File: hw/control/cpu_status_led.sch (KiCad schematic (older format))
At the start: 4 parts, among them Q401 BC817

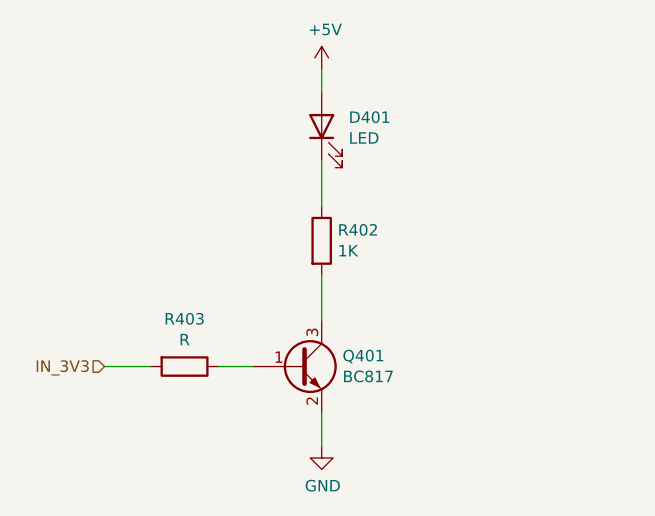
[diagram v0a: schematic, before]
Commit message: i[hw] Add IIS audio module connector
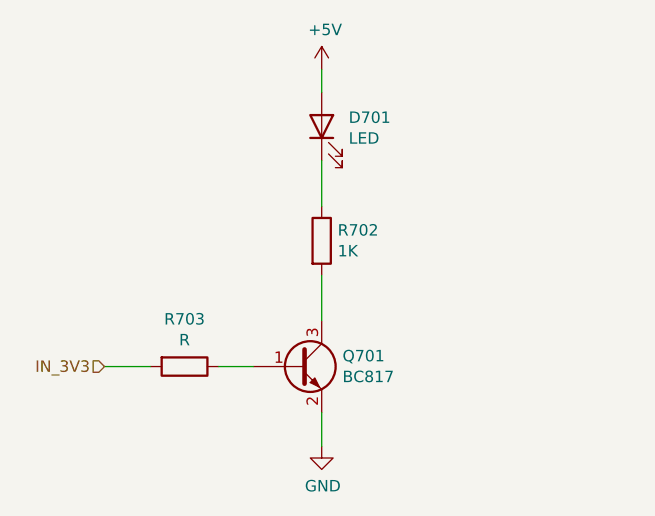
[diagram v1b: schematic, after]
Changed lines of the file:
@@
 AR Path="/6148E1AC/61836CD9/6182751A" Ref="#PWR0601"  Part="1"
 AR Path="/6148E1AC/61844B10/6182751A" Ref="#PWR0701"  Part="1"
-F 0 "#PWR0401" H 5500 2550 50  0001 C CNN
+F 0 "#PWR0701" H 5500 2550 50  0001 C CNN
 F 1 "+5V" H 5515 2873 50  0000 C CNN
 F 2 "" H 5500 2700 50  0001 C CNN
@@
 AR Path="/6148E1AC/61836CD9/6182D735" Ref="R603"  Part="1"
 AR Path="/6148E1AC/61844B10/6182D735" Ref="R703"  Part="1"
-F 0 "R403" V 4693 4000 50  0000 C CNN
+F 0 "R703" V 4693 4000 50  0000 C CNN
 F 1 "R" V 4784 4000 50  0000 C CNN
 F 2 "Resistor_SMD:R_0805_2012Metric_Pad1.20x1.40mm_HandSolder" V 4830 4000 50  0001 C CNN
@@
 AR Path="/6148E1AC/61836CD9/6182D73B" Ref="Q601"  Part="1"
 AR Path="/6148E1AC/61844B10/6182D73B" Ref="Q701"  Part="1"
-F 0 "Q401" H 5591 4046 50  0000 L CNN
+F 0 "Q701" H 5591 4046 50  0000 L CNN
 F 1 "BC817" H 5591 3955 50  0000 L CNN
 F 2 "Package_TO_SOT_SMD:SOT-23_Handsoldering" H 5600 4100 50  0001 C CNN
@@
 AR Path="/6148E1AC/61836CD9/6182D99B" Ref="D601"  Part="1"
 AR Path="/6148E1AC/61844B10/6182D99B" Ref="D701"  Part="1"
-F 0 "D401" V 5539 2832 50  0000 R CNN
+F 0 "D701" V 5539 2832 50  0000 R CNN
 F 1 "LED" V 5448 2832 50  0000 R CNN
 F 2 "LED_SMD:LED_0805_2012Metric_Pad1.15x1.40mm_HandSolder" H 5500 2950 50  0001 C CNN
@@
 AR Path="/6148E1AC/61836CD9/6182E435" Ref="R602"  Part="1"
 AR Path="/6148E1AC/61844B10/6182E435" Ref="R702"  Part="1"
-F 0 "R402" H 5570 3496 50  0000 L CNN
+F 0 "R702" H 5570 3496 50  0000 L CNN
 F 1 "1K" H 5570 3405 50  0000 L CNN
 F 2 "Resistor_SMD:R_0805_2012Metric_Pad1.20x1.40mm_HandSolder" V 5430 3450 50  0001 C CNN
@@
 AR Path="/6148E1AC/61836CD9/6182FC68" Ref="#PWR0602"  Part="1"
 AR Path="/6148E1AC/61844B10/6182FC68" Ref="#PWR0702"  Part="1"
-F 0 "#PWR0402" H 5500 4100 50  0001 C CNN
+F 0 "#PWR0702" H 5500 4100 50  0001 C CNN
 F 1 "GND" H 5505 4177 50  0000 C CNN
 F 2 "" H 5500 4350 50  0001 C CNN

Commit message: [hw] Add button, move sd card
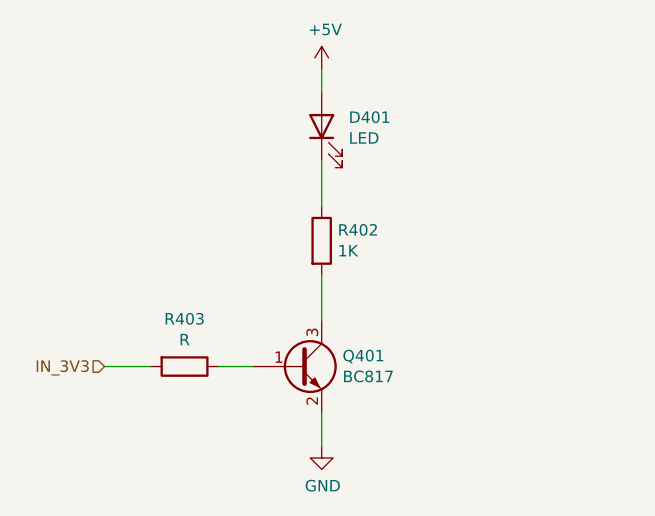
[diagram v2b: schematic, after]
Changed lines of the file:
@@
 AR Path="/6148E1AC/61836CD9/6182D735" Ref="R603"  Part="1"
 AR Path="/6148E1AC/61844B10/6182D735" Ref="R703"  Part="1"
-F 0 "R703" V 4693 4000 50  0000 C CNN
+F 0 "R403" V 4693 4000 50  0000 C CNN
 F 1 "R" V 4784 4000 50  0000 C CNN
 F 2 "Resistor_SMD:R_0805_2012Metric_Pad1.20x1.40mm_HandSolder" V 4830 4000 50  0001 C CNN
@@
 AR Path="/6148E1AC/61836CD9/6182D73B" Ref="Q601"  Part="1"
 AR Path="/6148E1AC/61844B10/6182D73B" Ref="Q701"  Part="1"
-F 0 "Q701" H 5591 4046 50  0000 L CNN
+F 0 "Q401" H 5591 4046 50  0000 L CNN
 F 1 "BC817" H 5591 3955 50  0000 L CNN
 F 2 "Package_TO_SOT_SMD:SOT-23_Handsoldering" H 5600 4100 50  0001 C CNN
@@
 AR Path="/6148E1AC/61836CD9/6182D99B" Ref="D601"  Part="1"
 AR Path="/6148E1AC/61844B10/6182D99B" Ref="D701"  Part="1"
-F 0 "D701" V 5539 2832 50  0000 R CNN
+F 0 "D401" V 5539 2832 50  0000 R CNN
 F 1 "LED" V 5448 2832 50  0000 R CNN
 F 2 "LED_SMD:LED_0805_2012Metric_Pad1.15x1.40mm_HandSolder" H 5500 2950 50  0001 C CNN
@@
 AR Path="/6148E1AC/61836CD9/6182E435" Ref="R602"  Part="1"
 AR Path="/6148E1AC/61844B10/6182E435" Ref="R702"  Part="1"
-F 0 "R702" H 5570 3496 50  0000 L CNN
+F 0 "R402" H 5570 3496 50  0000 L CNN
 F 1 "1K" H 5570 3405 50  0000 L CNN
 F 2 "Resistor_SMD:R_0805_2012Metric_Pad1.20x1.40mm_HandSolder" V 5430 3450 50  0001 C CNN

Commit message: [hw] Isolate SD card holder shield from ground
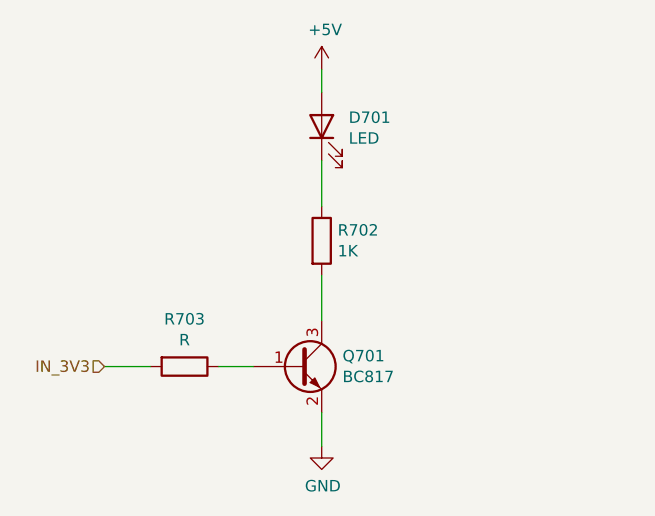
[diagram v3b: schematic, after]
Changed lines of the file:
@@
 AR Path="/6148E1AC/61836CD9/6182D735" Ref="R603"  Part="1"
 AR Path="/6148E1AC/61844B10/6182D735" Ref="R703"  Part="1"
-F 0 "R403" V 4693 4000 50  0000 C CNN
+F 0 "R703" V 4693 4000 50  0000 C CNN
 F 1 "R" V 4784 4000 50  0000 C CNN
 F 2 "Resistor_SMD:R_0805_2012Metric_Pad1.20x1.40mm_HandSolder" V 4830 4000 50  0001 C CNN
@@
 AR Path="/6148E1AC/61836CD9/6182D73B" Ref="Q601"  Part="1"
 AR Path="/6148E1AC/61844B10/6182D73B" Ref="Q701"  Part="1"
-F 0 "Q401" H 5591 4046 50  0000 L CNN
+F 0 "Q701" H 5591 4046 50  0000 L CNN
 F 1 "BC817" H 5591 3955 50  0000 L CNN
 F 2 "Package_TO_SOT_SMD:SOT-23_Handsoldering" H 5600 4100 50  0001 C CNN
@@
 AR Path="/6148E1AC/61836CD9/6182D99B" Ref="D601"  Part="1"
 AR Path="/6148E1AC/61844B10/6182D99B" Ref="D701"  Part="1"
-F 0 "D401" V 5539 2832 50  0000 R CNN
+F 0 "D701" V 5539 2832 50  0000 R CNN
 F 1 "LED" V 5448 2832 50  0000 R CNN
 F 2 "LED_SMD:LED_0805_2012Metric_Pad1.15x1.40mm_HandSolder" H 5500 2950 50  0001 C CNN
@@
 AR Path="/6148E1AC/61836CD9/6182E435" Ref="R602"  Part="1"
 AR Path="/6148E1AC/61844B10/6182E435" Ref="R702"  Part="1"
-F 0 "R402" H 5570 3496 50  0000 L CNN
+F 0 "R702" H 5570 3496 50  0000 L CNN
 F 1 "1K" H 5570 3405 50  0000 L CNN
 F 2 "Resistor_SMD:R_0805_2012Metric_Pad1.20x1.40mm_HandSolder" V 5430 3450 50  0001 C CNN

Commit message: [hw] Re-annotate all components
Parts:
- renumbered R402 to R401, R403 to R402
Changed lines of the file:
@@
 AR Path="/614AE8DA/6182D735" Ref="R?"  Part="1"
 AR Path="/614AB031/6182D735" Ref="R?"  Part="1"
-AR Path="/6148E1AC/6182662F/6182D735" Ref="R403"  Part="1"
-AR Path="/6148E1AC/61831583/6182D735" Ref="R503"  Part="1"
-AR Path="/6148E1AC/61836CD9/6182D735" Ref="R603"  Part="1"
-AR Path="/6148E1AC/61844B10/6182D735" Ref="R703"  Part="1"
-F 0 "R703" V 4693 4000 50  0000 C CNN
+AR Path="/6148E1AC/6182662F/6182D735" Ref="R402"  Part="1"
+AR Path="/6148E1AC/61831583/6182D735" Ref="R502"  Part="1"
+AR Path="/6148E1AC/61836CD9/6182D735" Ref="R602"  Part="1"
+AR Path="/6148E1AC/61844B10/6182D735" Ref="R702"  Part="1"
+F 0 "R702" V 4693 4000 50  0000 C CNN
 F 1 "R" V 4784 4000 50  0000 C CNN
 F 2 "Resistor_SMD:R_0805_2012Metric_Pad1.20x1.40mm_HandSolder" V 4830 4000 50  0001 C CNN
@@
 $EndComp
 $Comp
-L Device:R R402
+L Device:R R401
 U 1 1 6182E435
 P 5500 3450
-AR Path="/6148E1AC/6182662F/6182E435" Ref="R402"  Part="1"
-AR Path="/6148E1AC/61831583/6182E435" Ref="R502"  Part="1"
-AR Path="/6148E1AC/61836CD9/6182E435" Ref="R602"  Part="1"
-AR Path="/6148E1AC/61844B10/6182E435" Ref="R702"  Part="1"
-F 0 "R702" H 5570 3496 50  0000 L CNN
+AR Path="/6148E1AC/6182662F/6182E435" Ref="R401"  Part="1"
+AR Path="/6148E1AC/61831583/6182E435" Ref="R501"  Part="1"
+AR Path="/6148E1AC/61836CD9/6182E435" Ref="R601"  Part="1"
+AR Path="/6148E1AC/61844B10/6182E435" Ref="R701"  Part="1"
+F 0 "R701" H 5570 3496 50  0000 L CNN
 F 1 "1K" H 5570 3405 50  0000 L CNN
 F 2 "Resistor_SMD:R_0805_2012Metric_Pad1.20x1.40mm_HandSolder" V 5430 3450 50  0001 C CNN

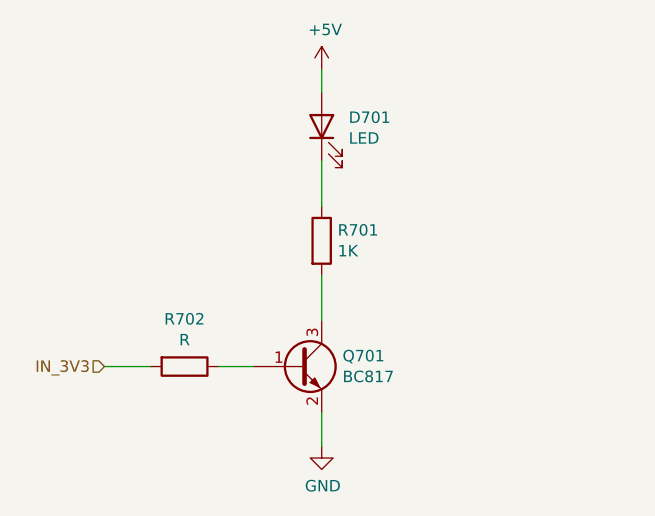
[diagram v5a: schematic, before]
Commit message: [hw] Add missing resistor values
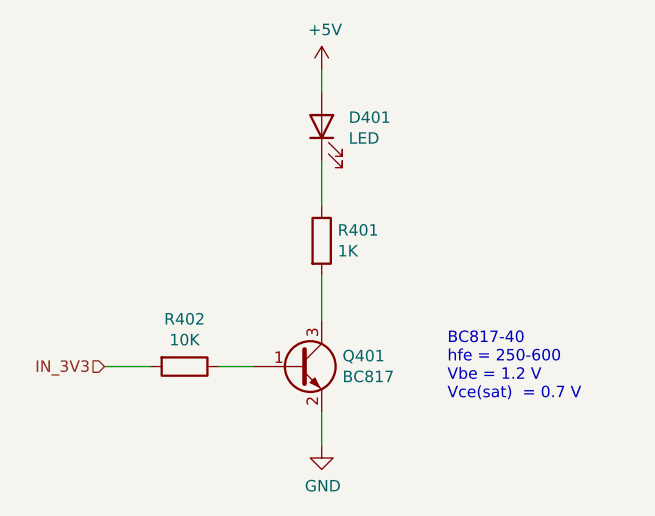
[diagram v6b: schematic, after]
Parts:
- R402: value R -> 10K
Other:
- note added: "BC817-40\nhfe = 250-600\nVbe = 1.2 V\nVce(sat) = 0.7 V"
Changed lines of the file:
@@
 AR Path="/6148E1AC/61836CD9/6182751A" Ref="#PWR0601"  Part="1"
 AR Path="/6148E1AC/61844B10/6182751A" Ref="#PWR0701"  Part="1"
-F 0 "#PWR0701" H 5500 2550 50  0001 C CNN
+F 0 "#PWR0401" H 5500 2550 50  0001 C CNN
 F 1 "+5V" H 5515 2873 50  0000 C CNN
 F 2 "" H 5500 2700 50  0001 C CNN
@@
 AR Path="/6148E1AC/61836CD9/6182D735" Ref="R602"  Part="1"
 AR Path="/6148E1AC/61844B10/6182D735" Ref="R702"  Part="1"
-F 0 "R702" V 4693 4000 50  0000 C CNN
-F 1 "R" V 4784 4000 50  0000 C CNN
+F 0 "R402" V 4693 4000 50  0000 C CNN
+F 1 "10K" V 4784 4000 50  0000 C CNN
 F 2 "Resistor_SMD:R_0805_2012Metric_Pad1.20x1.40mm_HandSolder" V 4830 4000 50  0001 C CNN
 F 3 "~" H 4900 4000 50  0001 C CNN
@@
 AR Path="/6148E1AC/61836CD9/6182D73B" Ref="Q601"  Part="1"
 AR Path="/6148E1AC/61844B10/6182D73B" Ref="Q701"  Part="1"
-F 0 "Q701" H 5591 4046 50  0000 L CNN
+F 0 "Q401" H 5591 4046 50  0000 L CNN
 F 1 "BC817" H 5591 3955 50  0000 L CNN
 F 2 "Package_TO_SOT_SMD:SOT-23_Handsoldering" H 5600 4100 50  0001 C CNN
@@
 AR Path="/6148E1AC/61836CD9/6182D99B" Ref="D601"  Part="1"
 AR Path="/6148E1AC/61844B10/6182D99B" Ref="D701"  Part="1"
-F 0 "D701" V 5539 2832 50  0000 R CNN
+F 0 "D401" V 5539 2832 50  0000 R CNN
 F 1 "LED" V 5448 2832 50  0000 R CNN
 F 2 "LED_SMD:LED_0805_2012Metric_Pad1.15x1.40mm_HandSolder" H 5500 2950 50  0001 C CNN
@@
 AR Path="/6148E1AC/61836CD9/6182E435" Ref="R601"  Part="1"
 AR Path="/6148E1AC/61844B10/6182E435" Ref="R701"  Part="1"
-F 0 "R701" H 5570 3496 50  0000 L CNN
+F 0 "R401" H 5570 3496 50  0000 L CNN
 F 1 "1K" H 5570 3405 50  0000 L CNN
 F 2 "Resistor_SMD:R_0805_2012Metric_Pad1.20x1.40mm_HandSolder" V 5430 3450 50  0001 C CNN
@@
 AR Path="/6148E1AC/61836CD9/6182FC68" Ref="#PWR0602"  Part="1"
 AR Path="/6148E1AC/61844B10/6182FC68" Ref="#PWR0702"  Part="1"
-F 0 "#PWR0702" H 5500 4100 50  0001 C CNN
+F 0 "#PWR0402" H 5500 4100 50  0001 C CNN
 F 1 "GND" H 5505 4177 50  0000 C CNN
 F 2 "" H 5500 4350 50  0001 C CNN
@@
 Wire Wire Line
 	4550 4000 4750 4000
+Text Notes 6050 4150 0    50   ~ 0
+BC817-40\nhfe = 250-600\nVbe = 1.2 V\nVce(sat)  = 0.7 V
 $EndSCHEMATC
